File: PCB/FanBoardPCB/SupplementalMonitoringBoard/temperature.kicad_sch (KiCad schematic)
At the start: 11 parts, among them U3 OPA842xDBV

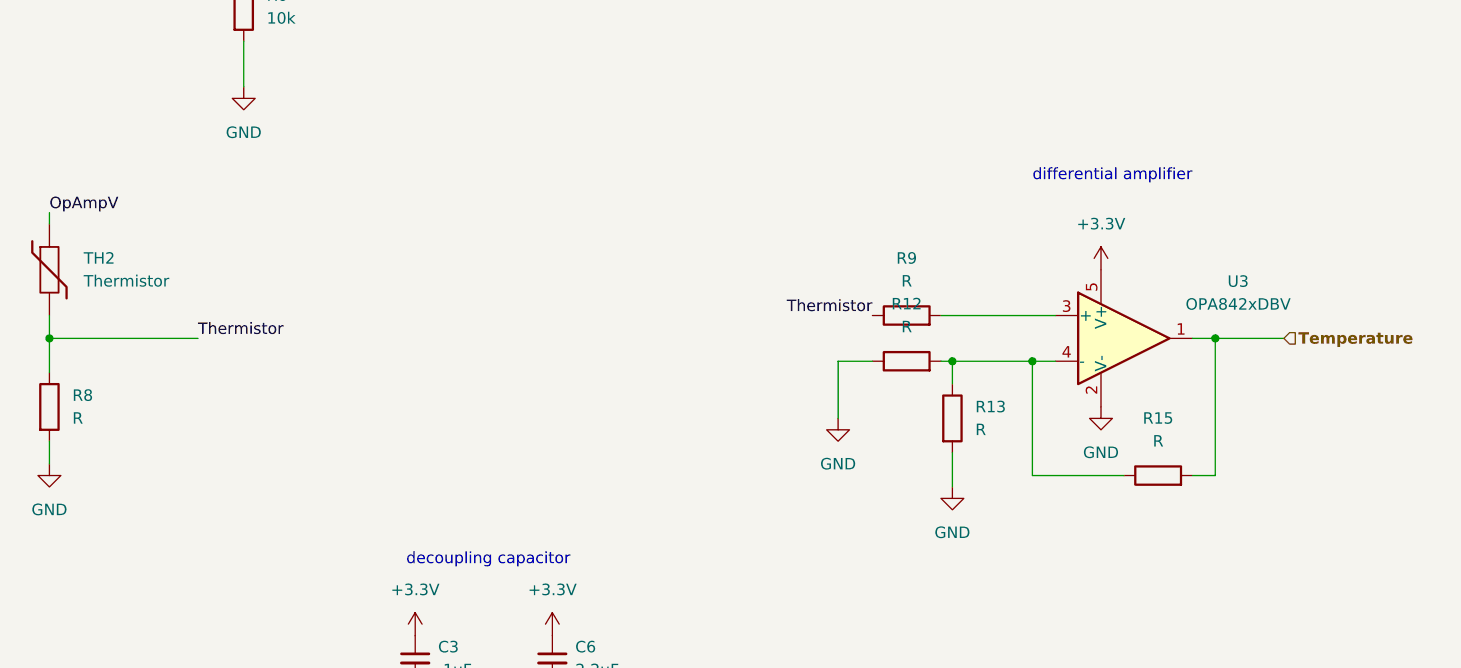
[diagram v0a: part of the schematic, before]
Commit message: Supplemental Monitoring Board
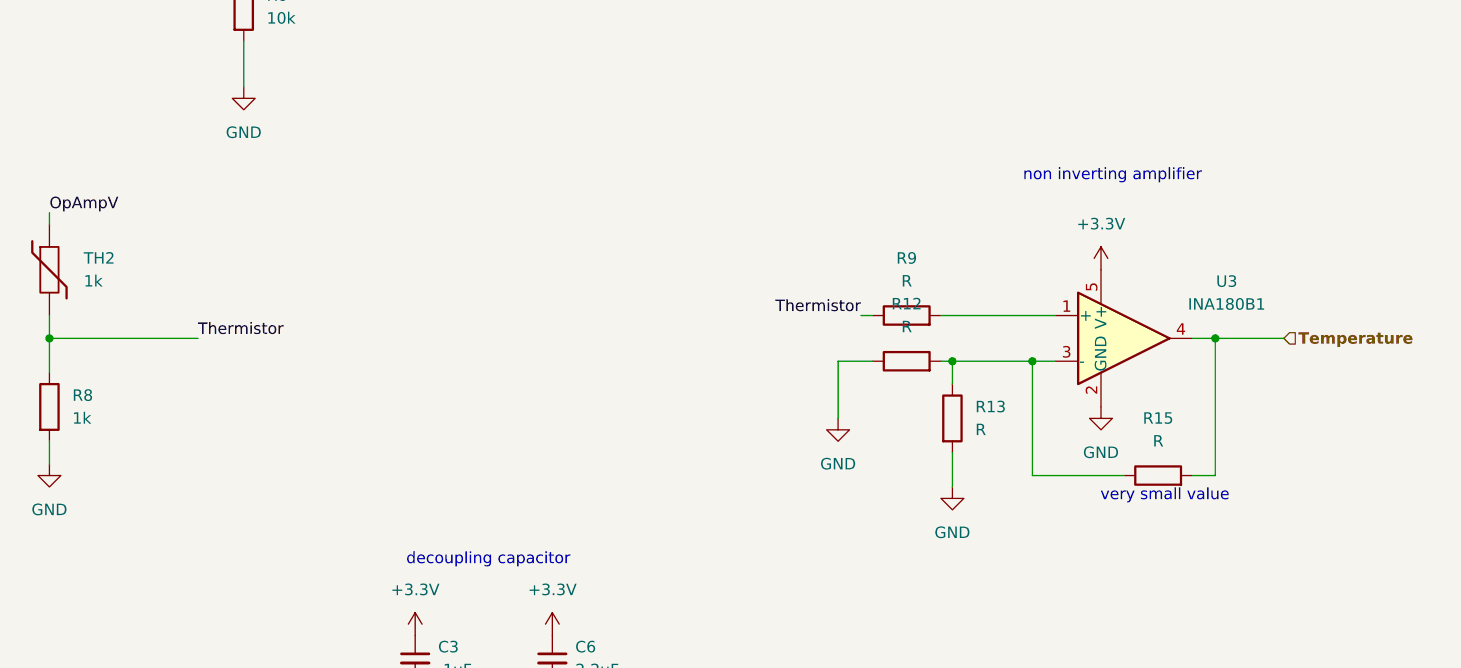
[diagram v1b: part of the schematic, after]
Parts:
- removed U3: OPA842xDBV, Package_TO_SOT_SMD:SOT-23-5, symbol Amplifier_Operational:OPA842xDBV
- added U3: INA180B1, Package_TO_SOT_SMD:SOT-23-5, symbol Amplifier_Current:INA180B1
- R8: value R -> 1k
- TH2: value Thermistor -> 1k
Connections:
- net +3.3V: now also U3.5 (V+)
- net GND: now also U3.2 (GND)
- net Temperature: now also U3.4
- net at R9.2: now also U3.1 (+)
- net at R12.2, R13.1, R15.1: now also U3.3 (-)
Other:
- note added: "non inverting amplifier"
- note added: "very small value"
- note removed: "differential amplifier"
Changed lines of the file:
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@@
+	(wire
+		(pts
+			(xy 121.92 91.44) (xy 123.19 91.44)
+		)
+		(stroke
+			(width 0)
+			(type default)
+		)
+	)
 	(wire
 		(pts
@@
 		)
 	)
-	(text "differential amplifier"
+	(text "non inverting amplifier"
 		(exclude_from_sim no)
 		(at 149.86 75.946 0)
@@
 				(thickness 0.1746)
 				(color 132 0 0 1)
+			)
+		)
+	)
+	(text "very small value\n"
+		(exclude_from_sim no)
+		(at 155.702 111.506 0)
+		(effects
+			(font
+				(size 1.27 1.27)
 			)
 		)
@@
 	)
 	(label "Thermistor"
-		(at 123.19 91.44 180)
+		(at 121.92 91.44 180)
 		(fields_autoplaced yes)
 		(effects
@@
 			)
 		)
-		(property "Value" "Thermistor"
+		(property "Value" "1k"
 			(at 35.56 87.6299 0)
 			(effects
@@
 			)
 		)
-		(property "Value" "R"
+		(property "Value" "1k"
 			(at 34.29 102.8699 0)
 			(effects
@@
 	)
 	(symbol
+		(lib_id "Amplifier_Current:INA180B1")
+		(at 151.13 93.98 0)
+		(unit 1)
+		(exclude_from_sim no)
+		(in_bom yes)
+		(on_board yes)
+		(dnp no)
+		(fields_autoplaced yes)
+		(property "Reference" "U3"
+			(at 162.56 87.6614 0)
+			(effects
+				(font
+					(size 1.27 1.27)
+				)
+			)
+		)
+		(property "Value" "INA180B1"
+			(at 162.56 90.2014 0)
+			(effects
+				(font
+					(size 1.27 1.27)
+				)
+			)
+		)
+		(property "Footprint" "Package_TO_SOT_SMD:SOT-23-5"
+			(at 152.4 92.71 0)
+			(effects
+				(font
+					(size 1.27 1.27)
+				)
+				(hide yes)
+			)
+		)
+		(property "Datasheet" "http://www.ti.com/lit/ds/symlink/ina180.pdf"
+			(at 154.94 90.17 0)
+			(effects
+				(font
+					(size 1.27 1.27)
+				)
+				(hide yes)
+			)
+		)
+		(property "Description" "Current Sense Amplifier, 1 Circuit, Rail-to-Rail, 26V, Gain 20 V/V, SOT-23-5"
+			(at 151.13 93.98 0)
+			(effects
+				(font
+					(size 1.27 1.27)
+				)
+				(hide yes)
+			)
+		)
+		(pin "1"
+		)
+		(pin "2"
+		)
+		(pin "4"
+		)
+		(pin "5"
+		)
+		(pin "3"
+		)
+		(instances
+			(project ""
+				(path "/aa0415d0-3287-4bc4-9a8e-766ada9ace2f/cde5a840-cd97-4154-b488-bad27326129c"
+					(reference "U3")
+					(unit 1)
+				)
+			)
+		)
+	)
+	(symbol
 		(lib_id "power:GND")
 		(at 72.39 132.08 0)
@@
 					(unit 1)
 				)
-			)
-		)
-	)
-	(symbol
-		(lib_id "Amplifier_Operational:OPA842xDBV")
-		(at 151.13 93.98 0)
-		(unit 1)
-		(exclude_from_sim no)
-		(in_bom yes)
-		(on_board yes)
-		(dnp no)
-		(fields_autoplaced yes)
-		(property "Reference" "U3"
-			(at 163.83 87.6614 0)
-			(effects
-				(font
-					(size 1.27 1.27)
-				)
-			)
-		)
-		(property "Value" "OPA842xDBV"
-			(at 163.83 90.2014 0)
-			(effects
-				(font
-					(size 1.27 1.27)
-				)
-			)
-		)
-		(property "Footprint" "Package_TO_SOT_SMD:SOT-23-5"
-			(at 148.59 99.06 0)
-			(effects
-				(font
-					(size 1.27 1.27)
-				)
-				(justify left)
-				(hide yes)
-			)
-		)
-		(property "Datasheet" "http://www.ti.com/lit/ds/symlink/opa842.pdf"
-			(at 151.13 88.9 0)
-			(effects
-				(font
-					(size 1.27 1.27)
-				)
-				(hide yes)
-			)
-		)
-		(property "Description" "200MHz, Low Distortion, Unity-Gain Stable, Voltage Feedback Operational Amplifier, SOT23-5"
-			(at 151.13 93.98 0)
-			(effects
-				(font
-					(size 1.27 1.27)
-				)
-				(hide yes)
-			)
-		)
-		(pin "2"
-		)
-		(pin "3"
-		)
-		(pin "1"
-		)
-		(pin "5"
-		)
-		(pin "4"
-		)
-		(instances
-			(project "SupplementalMonitoringBoard"
-				(path "/aa0415d0-3287-4bc4-9a8e-766ada9ace2f/cde5a840-cd97-4154-b488-bad27326129c"
-					(reference "U3")
-					(unit 1)
-				)
